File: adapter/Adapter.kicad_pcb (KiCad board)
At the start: 4 copper layers, 33.1 x 18.6 mm, 13 parts, among them J1 USB_B_Micro, J2 2040210-1, J3 USB_C_Receptacle

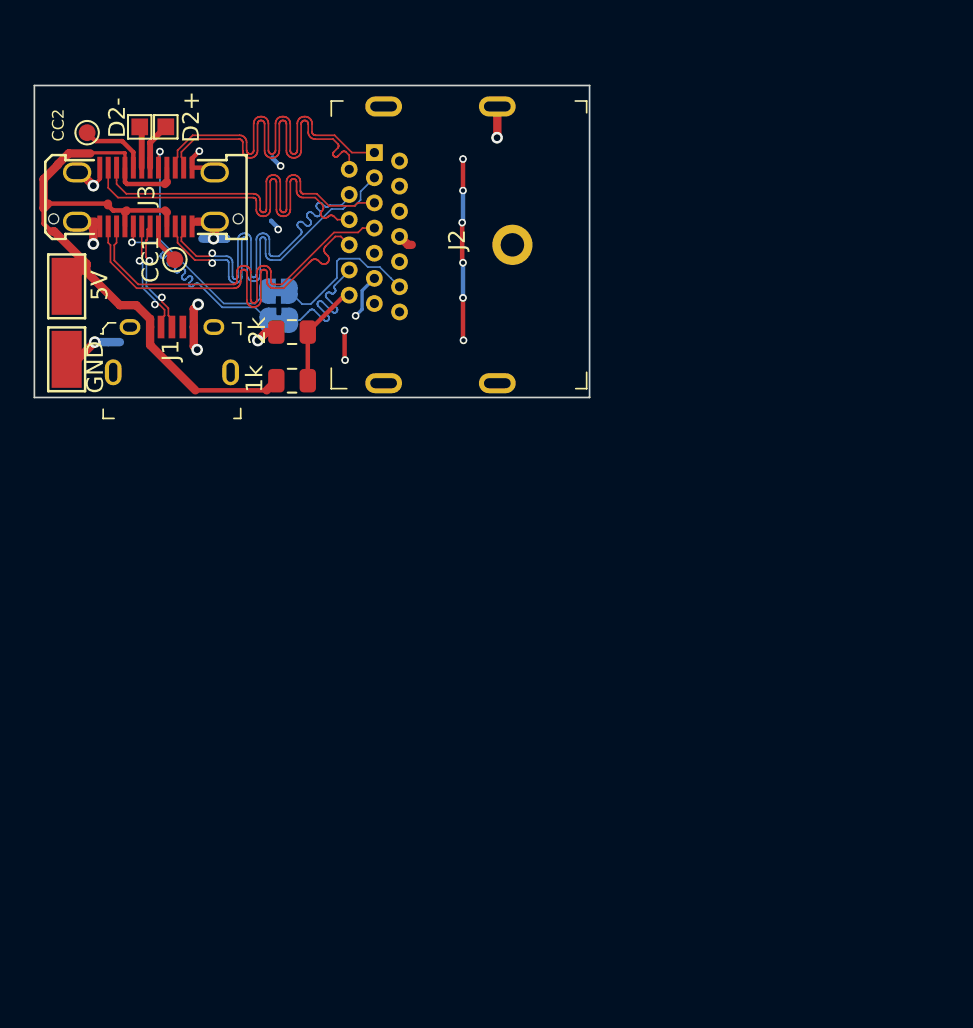
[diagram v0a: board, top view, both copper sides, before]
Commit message: Design considerations and fixed most external circuitry for STM32
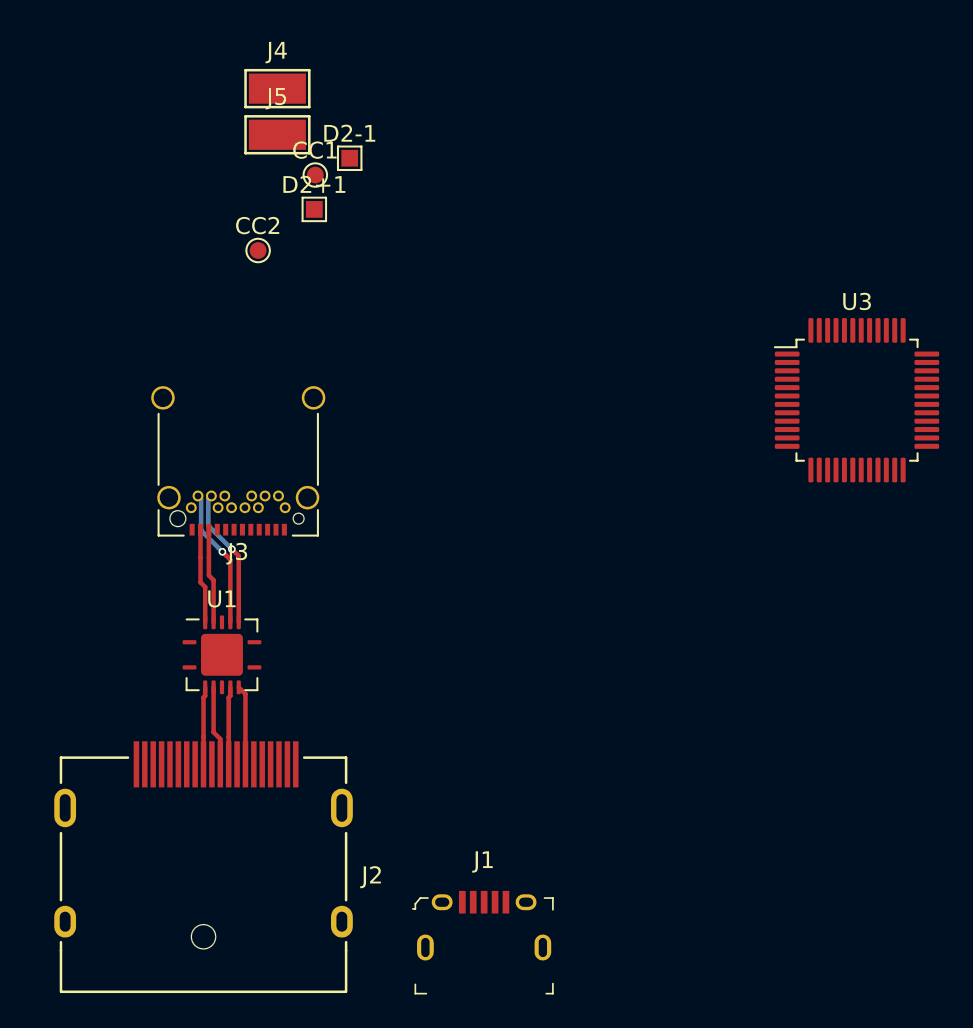
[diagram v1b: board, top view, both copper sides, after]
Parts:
- removed 1k: 1k, Resistor_SMD:R_0805_2012Metric
- removed 2k: 2k, Resistor_SMD:R_0805_2012Metric
- removed 5V, GND: Conn_01x01, TestPoint:TestPoint_Keystone_5015_Micro-Minature
- removed AUX+, AUX-: Jumper, Jumper:SolderJumper-2_P1.3mm_Bridged_RoundedPad1.0x1.5mm
- removed D2+, D2-: Conn_01x01, TestPoint:TestPoint_Pad_1.0x1.0mm
- added D2+1: Conn_01x01, TestPoint:TestPoint_Pad_1.0x1.0mm, F.Cu at (32.5, 21.8)
- added D2-1: Conn_01x01, TestPoint:TestPoint_Pad_1.0x1.0mm, F.Cu at (34.6, 18.8)
- added J4: Conn_01x01, TestPoint:TestPoint_Keystone_5015_Micro-Minature, F.Cu at (30.3, 14.6)
- added J5: Conn_01x01, TestPoint:TestPoint_Keystone_5015_Micro-Minature, F.Cu at (30.3, 17.4)
- added U1: SN75DP119, SN75DP118:QFN-20-1EP_4x4mm_P0.5mm_EP2.5x2.5mm, F.Cu at (27.0, 48.4)
- added U3: STM32F072C8Tx, Package_QFP:LQFP-48_7x7mm_P0.5mm, F.Cu at (64.9, 33.2)
- J2: footprint digikey-footprints:DisplayPort_2040210-1 -> DP1RD20JQ1R400:DP1RD20JQ1R400
- J3: footprint USB_C:DX07S024WJ3R400 -> Connector_USB:USB_C_Receptacle_Amphenol_12401548E4-2A_CircularHoles
- moved J1 39.0 mm to (42.6, 63.1)
- moved J2 38.3 mm to (25.9, 57.5), turned to 0 degrees
- moved J3 14.6 mm to (28.0, 35.9)
- moved CC2 12.4 mm to (29.2, 24.3), turned to 0 degrees
- moved CC1 9.78 mm to (32.6, 19.8), turned to 0 degrees
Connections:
- J2 pad 1: /DP3- -> /DP_IN_3-
- J2 pad 10: /DP0- -> /DP_IN_0-
- J2 pad 12: /DP0+ -> /DP_IN_0+
- J2 pad 3: /DP3+ -> /DP_IN_3+
- J2 pad 4: /DP2- -> /DP_IN_2-
- J2 pad 6: /DP2+ -> /DP_IN_2+
- J2 pad 7: /DP1- -> /DP_IN_1-
- J2 pad 9: /DP1+ -> /DP_IN_1+
- J3 pad A10: /DP0- -> /DP_OUT_0-
- J3 pad A11: /DP0+ -> /DP_OUT_0+
- J3 pad A2: /DP2+ -> Net-(J3-PadA2)
- J3 pad A3: /DP2- -> Net-(J3-PadA3)
- J3 pad A8: /pAUX+ -> /AUX+
- J3 pad B10: /DP3- -> Net-(J3-PadB10)
- J3 pad B11: /DP3+ -> Net-(J3-PadB11)
- J3 pad B2: /DP1+ -> /DP_OUT_1+
- J3 pad B3: /DP1- -> /DP_OUT_1-
- J3 pad B6: /D2+ -> /D+
- J3 pad B7: /D2- -> /D-
- J3 pad B8: /pAUX- -> /AUX-
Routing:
- net VBUS: track 44.2 -> 0.00 mm
- net GND: track 41.0 -> 0.00 mm, vias 20 -> 0
- net /DP0+: track 25.3 -> 0.00 mm
- net /DP0-: track 25.3 -> 0.00 mm
- net /DP2-: track 25.2 -> 0.00 mm, vias 1 -> 0
- net /DP2+: track 25.2 -> 0.00 mm, vias 1 -> 0
- net /DP3+: track 25.1 -> 0.00 mm
- net /DP3-: track 25.1 -> 0.00 mm
- net /DP1+: track 24.8 -> 0.00 mm
- net /DP1-: track 24.6 -> 0.00 mm
- net /pAUX+: track 14.5 -> 0.00 mm, vias 1 -> 0
- net /pAUX-: track 14.5 -> 0.00 mm, vias 1 -> 0
- net /AUX+: track 9.34 -> 0.00 mm
- net /AUX-: track 9.29 -> 0.00 mm
- net /DP_OUT_1-: track 0.00 -> 8.36 mm, vias 0 -> 1
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- removed copper zone on In1.Cu, net GND
- removed copper zone on In2.Cu, net GND
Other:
- board outline removed

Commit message: cleared a bunch of questions
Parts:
- removed J5: Conn_01x01, TestPoint:TestPoint_Keystone_5015_Micro-Minature
- added R8: NF, Resistor_SMD:R_0603_1608Metric_Pad1.05x0.95mm_HandSolder, F.Cu at (44.7, 47.3)
- added R9: NF, Resistor_SMD:R_0603_1608Metric_Pad1.05x0.95mm_HandSolder, F.Cu at (48.1, 45.8)
- J4: value Conn_01x01 -> Conn_01x05_Male
- moved U3 30.6 mm to (37.7, 47.3)
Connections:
- net Net-(U3-Pad21) renamed VBUS_EN
- net Net-(U3-Pad7) renamed /nRESET
- J2 pad 13: /CONFIG1 -> CONFIG1
- J2 pad 14: /CONFIG2 -> CONFIG2
- J3 pad A4: VBUS -> Net-(J3-PadA4)
- J3 pad A9: VBUS -> Net-(J3-PadA4)
- J3 pad B4: VBUS -> Net-(J3-PadA4)
- J3 pad B9: VBUS -> Net-(J3-PadA4)
- J4 pad 1: VBUS -> /EXT_3.3V
- U3 pad 1: Net-(U3-Pad1) -> Net-(C5-Pad2)
- U3 pad 24: Net-(U3-Pad24) -> Net-(C5-Pad2)
- U3 pad 30: Net-(U3-Pad30) -> /HPD
- U3 pad 36: Net-(U3-Pad36) -> Net-(C5-Pad2)
- U3 pad 45: Net-(U3-Pad45) -> CONFIG2
- U3 pad 46: Net-(U3-Pad46) -> CONFIG1
- U3 pad 48: Net-(U3-Pad48) -> Net-(C5-Pad2)
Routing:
- net /D+: track 0.00 -> 45.3 mm
- net /D-: track 0.00 -> 44.7 mm

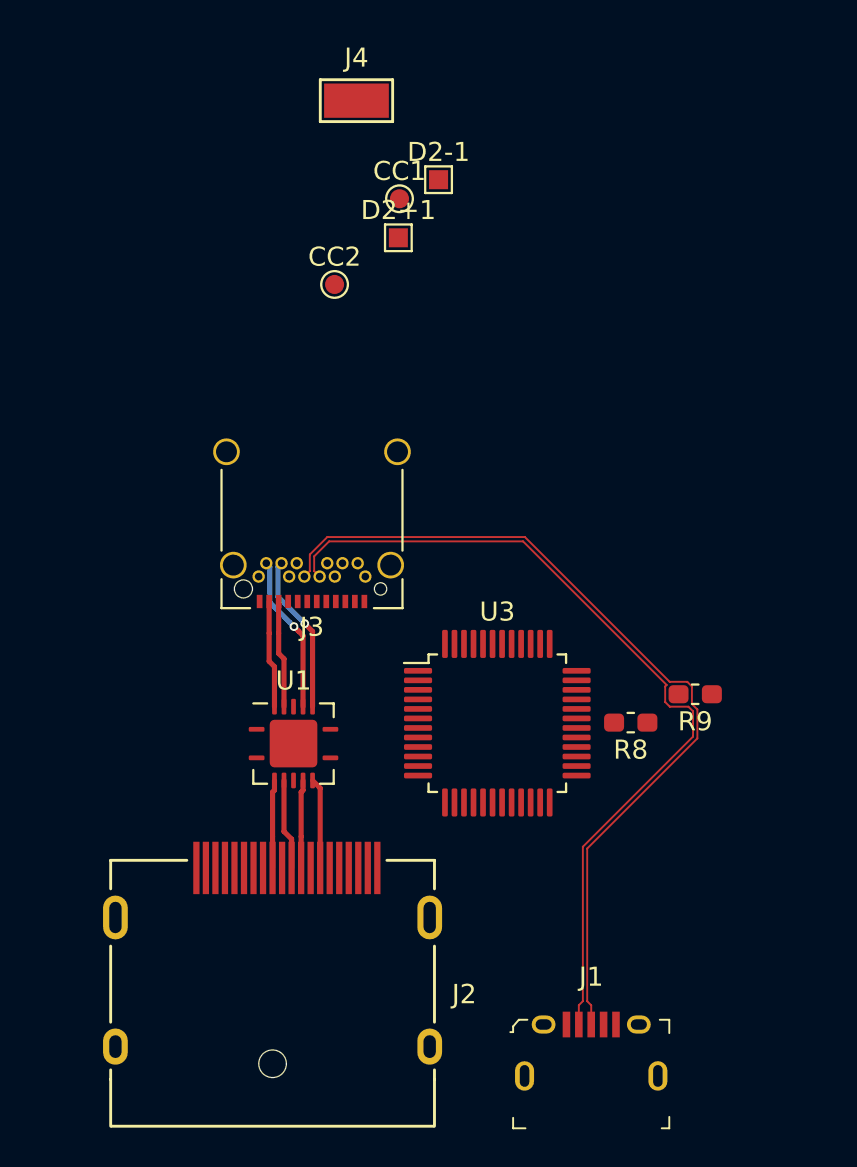
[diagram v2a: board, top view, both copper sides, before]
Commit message: pre-place most of components
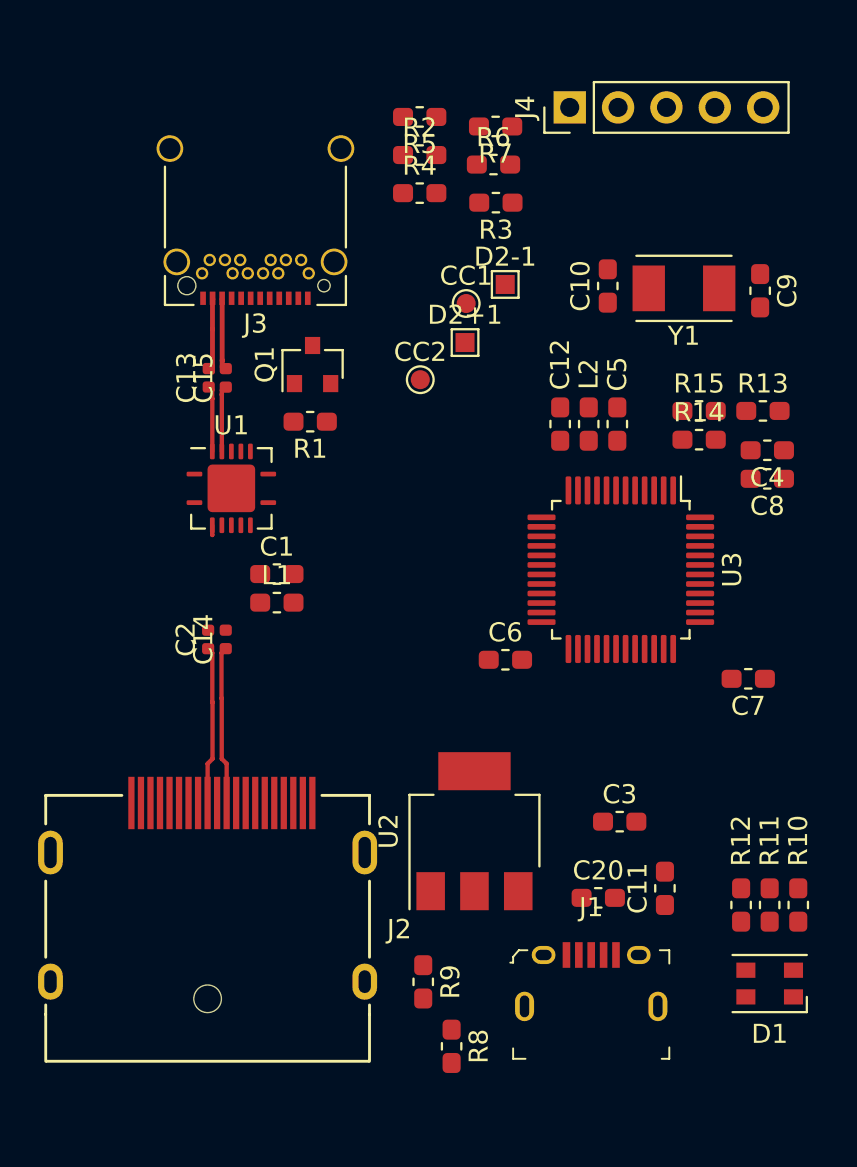
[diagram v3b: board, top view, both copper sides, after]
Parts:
- added C1: 100n, Capacitor_SMD:C_0603_1608Metric_Pad1.05x0.95mm_HandSolder, F.Cu at (26.1, 39.5)
- added C10: 20p, Capacitor_SMD:C_0603_1608Metric_Pad1.05x0.95mm_HandSolder, F.Cu at (43.5, 24.4)
- added C11: 4u7, Capacitor_SMD:C_0603_1608Metric_Pad1.05x0.95mm_HandSolder, F.Cu at (46.5, 56.0)
- added C12: 1u, Capacitor_SMD:C_0603_1608Metric_Pad1.05x0.95mm_HandSolder, F.Cu at (41.0, 31.6)
- added C13: 100n, Capacitor_SMD:C_0402_1005Metric, F.Cu at (22.5, 29.2)
- added C14: 100n, Capacitor_SMD:C_0402_1005Metric, F.Cu at (23.4, 42.9)
- added C15: 100n, Capacitor_SMD:C_0402_1005Metric, F.Cu at (23.4, 29.2)
- added C2: 100n, Capacitor_SMD:C_0402_1005Metric, F.Cu at (22.5, 42.9)
- added C20: 4u7, Capacitor_SMD:C_0603_1608Metric_Pad1.05x0.95mm_HandSolder, F.Cu at (43.0, 56.5)
- added C3: 4u7, Capacitor_SMD:C_0603_1608Metric_Pad1.05x0.95mm_HandSolder, F.Cu at (44.1, 52.5)
- added C4: 100n, Capacitor_SMD:C_0603_1608Metric_Pad1.05x0.95mm_HandSolder, F.Cu at (51.9, 33.0)
- added C5: 100n, Capacitor_SMD:C_0603_1608Metric_Pad1.05x0.95mm_HandSolder, F.Cu at (44.0, 31.6)
- added C6: 100n, Capacitor_SMD:C_0603_1608Metric_Pad1.05x0.95mm_HandSolder, F.Cu at (38.1, 44.0)
- added C7: 100n, Capacitor_SMD:C_0603_1608Metric_Pad1.05x0.95mm_HandSolder, F.Cu at (50.9, 45.0)
- added C8: 100n, Capacitor_SMD:C_0603_1608Metric_Pad1.05x0.95mm_HandSolder, F.Cu at (51.9, 34.5)
- added C9: 20p, Capacitor_SMD:C_0603_1608Metric_Pad1.05x0.95mm_HandSolder, F.Cu at (51.5, 24.6)
- added D1: LED_ARGB, LED_SMD:LED_Cree-PLCC4_3.2x2.8mm_CCW, F.Cu at (52.0, 61.0)
- added L1: CIM05U601NC, Inductor_SMD:L_0603_1608Metric_Pad1.05x0.95mm_HandSolder, F.Cu at (26.1, 41.0)
- added L2: CIM05U601NC, Inductor_SMD:L_0603_1608Metric_Pad1.05x0.95mm_HandSolder, F.Cu at (42.5, 31.6)
- added Q1: IRLML2244TRPBF, Package_TO_SOT_SMD:SOT-23, F.Cu at (28.0, 28.5)
- added R1: 100k, Resistor_SMD:R_0603_1608Metric_Pad1.05x0.95mm_HandSolder, F.Cu at (27.9, 31.5)
- added R10: R, Resistor_SMD:R_0603_1608Metric_Pad1.05x0.95mm_HandSolder, F.Cu at (53.5, 56.9)
- added R11: R, Resistor_SMD:R_0603_1608Metric_Pad1.05x0.95mm_HandSolder, F.Cu at (52.0, 56.9)
- added R12: R, Resistor_SMD:R_0603_1608Metric_Pad1.05x0.95mm_HandSolder, F.Cu at (50.5, 56.9)
- added R13: R, Resistor_SMD:R_0603_1608Metric_Pad1.05x0.95mm_HandSolder, F.Cu at (51.6, 30.9)
- added R14: R, Resistor_SMD:R_0603_1608Metric_Pad1.05x0.95mm_HandSolder, F.Cu at (48.3, 32.4)
- added R15: R, Resistor_SMD:R_0603_1608Metric_Pad1.05x0.95mm_HandSolder, F.Cu at (48.3, 30.9)
- added R2: <5k?, Resistor_SMD:R_0603_1608Metric_Pad1.05x0.95mm_HandSolder, F.Cu at (33.6, 17.5)
- added R3: <5k?, Resistor_SMD:R_0603_1608Metric_Pad1.05x0.95mm_HandSolder, F.Cu at (37.6, 20.0)
- added R4: 200, Resistor_SMD:R_0603_1608Metric_Pad1.05x0.95mm_HandSolder, F.Cu at (33.6, 19.5)
- added R5: 100, Resistor_SMD:R_0603_1608Metric_Pad1.05x0.95mm_HandSolder, F.Cu at (33.6, 15.5)
- added R6: 200, Resistor_SMD:R_0603_1608Metric_Pad1.05x0.95mm_HandSolder, F.Cu at (37.5, 18.0)
- added R7: 100, Resistor_SMD:R_0603_1608Metric_Pad1.05x0.95mm_HandSolder, F.Cu at (37.6, 16.0)
- added U2: AZ1117-3.3, Package_TO_SOT_SMD:SOT-223, F.Cu at (36.5, 53.0)
- added Y1: 8MHZ, Crystal:Crystal_SMD_TXC_7A-2Pin_5x3.2mm, F.Cu at (47.5, 24.5)
- J4: footprint TestPoint:TestPoint_Keystone_5015_Micro-Minature -> Connector_PinHeader_2.54mm:PinHeader_1x05_P2.54mm_Vertical
- moved R9 20.8 mm to (33.8, 60.9), turned to 270 degrees
- moved R8 19.4 mm to (35.3, 64.3), turned to 270 degrees
- moved J3 16.2 mm to (25.0, 20.0)
- moved U1 13.8 mm to (23.7, 35.0)
- moved J4 11.2 mm to (41.5, 15.0), turned to 90 degrees
- moved U3 10.3 mm to (44.2, 39.3), turned to 270 degrees
- moved CC2 6.73 mm to (33.7, 29.3)
- moved CC1 6.52 mm to (36.1, 25.3)
- moved D2+1 6.52 mm to (36.0, 27.3)
- moved D2-1 6.52 mm to (38.1, 24.3)
- moved J2 4.82 mm to (22.5, 54.1)
- moved J1 3.65 mm to (42.6, 59.5)
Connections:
- net Net-(C5-Pad2) renamed +3V3
- net Net-(U3-Pad31) renamed /UART_RX
- U1 pad 10: /DP_OUT_1+ -> Net-(U1-Pad10)
- U1 pad 12: /DP_OUT_0- -> Net-(C15-Pad1)
- U1 pad 13: /DP_OUT_0+ -> Net-(C13-Pad1)
- U1 pad 2: /DP_IN_0+ -> Net-(C2-Pad2)
- U1 pad 3: /DP_IN_0- -> Net-(C14-Pad2)
- U1 pad 5: /DP_IN_1+ -> Net-(U1-Pad5)
- U1 pad 6: /DP_IN_1- -> Net-(U1-Pad6)
- U1 pad 9: /DP_OUT_1- -> Net-(U1-Pad9)
- U3 pad 10: Net-(U3-Pad10) -> /CC1_EN
- U3 pad 11: Net-(U3-Pad11) -> /CC1_RX
- U3 pad 12: Net-(U3-Pad12) -> /CC2_EN
- U3 pad 13: Net-(U3-Pad13) -> /CC2_RX
- U3 pad 14: Net-(U3-Pad14) -> PRE_CTL
- U3 pad 15: Net-(U3-Pad15) -> /TX_CLK
- U3 pad 16: Net-(U3-Pad16) -> /CC2_TX
- U3 pad 17: Net-(U3-Pad17) -> VOD_CTL
- U3 pad 18: Net-(U3-Pad18) -> EQ_CTL
- U3 pad 19: Net-(U3-Pad19) -> EN_CTL
- U3 pad 22: Net-(U3-Pad22) -> /LED_G_L
- U3 pad 23: Net-(U3-Pad23) -> GND
- U3 pad 26: Net-(U3-Pad26) -> /LED_R_L
- U3 pad 27: Net-(U3-Pad27) -> /LED_B_L
- U3 pad 29: Net-(U3-Pad29) -> /HPD
- U3 pad 30: /HPD -> /UART_TX
- U3 pad 35: Net-(U3-Pad35) -> GND
- U3 pad 40: Net-(U3-Pad40) -> /CC1_TX
- U3 pad 43: Net-(U3-Pad43) -> CONFIG1
- U3 pad 44: Net-(U3-Pad44) -> /BOOT
- U3 pad 46: CONFIG1 -> /TX_CLK
- U3 pad 47: Net-(U3-Pad47) -> GND
- U3 pad 8: Net-(U3-Pad8) -> GND
- U3 pad 9: Net-(C6-Pad2) -> VDDA
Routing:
- net /D+: track 45.3 -> 0.00 mm
- net /D-: track 44.7 -> 0.00 mm
- net /DP_OUT_1-: track 8.36 -> 0.00 mm, vias 1 -> 0
- net /DP_OUT_1+: track 8.33 -> 0.00 mm, vias 1 -> 0
- net /DP_IN_1-: track 4.76 -> 0.00 mm
- net /DP_IN_1+: track 4.63 -> 0.00 mm
- net /DP_IN_0+: track 4.63 -> 8.30 mm
- net Net-(C15-Pad1): track 0.00 -> 3.61 mm
- net Net-(C13-Pad1): track 0.00 -> 3.58 mm
- net /DP_IN_0-: track 4.76 -> 8.31 mm
- net /DP_OUT_0-: track 5.64 -> 3.48 mm
- net /DP_OUT_0+: track 5.64 -> 4.06 mm
- net Net-(C2-Pad2): track 0.00 -> 0.51 mm
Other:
- net class DisplayPort added: clearance 0.127, trace_width 0.2286, via_dia 0.46, via_drill 0.26
- net class Power removed

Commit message: Added 3D STEP for micro-USB Jack
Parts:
- removed D2+1, D2-1: Conn_01x01, TestPoint:TestPoint_Pad_1.0x1.0mm
- added C16: 100n, Capacitor_SMD:C_0603_1608Metric_Pad1.05x0.95mm_HandSolder, F.Cu at (41.2, 24.3)
- added R16: 390, Resistor_SMD:R_0603_1608Metric_Pad1.05x0.95mm_HandSolder, F.Cu at (52.1, 32.0)
- added SW1: SW_Push, Button_Switch_SMD:SW_SPST_PTS645, F.Cu at (47.8, 23.0)
- moved J4 37.9 mm to (15.8, 42.8), turned to 180 degrees
- moved R8 30.5 mm to (30.3, 34.2), turned to 0 degrees
- moved R9 25.2 mm to (31.6, 35.8), turned to 0 degrees
- moved C7 17.9 mm to (33.4, 41.3), turned to 90 degrees
- moved C9 17.1 mm to (52.2, 41.7), turned to 180 degrees
- moved C6 15.9 mm to (34.4, 28.5), turned to 270 degrees
- moved Y1 14.0 mm to (52.1, 37.7), turned to 90 degrees
- moved C10 12.8 mm to (52.2, 33.7), turned to 0 degrees
- moved R13 11.9 mm to (47.5, 42.0), turned to 270 degrees
- moved C4 11.3 mm to (45.4, 42.3), turned to 90 degrees
- moved C8 11.1 mm to (43.9, 42.3), turned to 90 degrees
- moved R15 7.80 mm to (47.5, 38.7), turned to 270 degrees
- moved CC2 7.77 mm to (37.6, 22.6)
- moved U3 6.89 mm to (39.1, 34.6), turned to 180 degrees
- moved C20 6.77 mm to (46.1, 50.5)
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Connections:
- U3 pad 6: Net-(C10-Pad1) -> Net-(R16-Pad1)
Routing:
- net /D-: track 0.00 -> 28.7 mm, vias 0 -> 1
- net /D+: track 0.00 -> 28.6 mm
- net Net-(C2-Pad2): track 0.51 -> 6.12 mm
- net Net-(C14-Pad2): track 0.00 -> 5.59 mm
- net Net-(C1-Pad1): track 0.00 -> 4.69 mm

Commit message: Step file for MicroUSB
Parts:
- added R17: 0, Resistor_SMD:R_0603_1608Metric_Pad1.05x0.95mm_HandSolder, F.Cu at (43.8, 47.7)
- added SW2: SW_Push, Button_Switch_SMD:SW_SPST_PTS645, F.Cu at (-47.1, -2.67)
- J1: footprint digikey-footprints:USB_Micro_B_Female_10118194-0001LF -> USB_MicroB:CONN-10118194-0001LF-FCI
- J3: footprint Connector_USB:USB_C_Receptacle_Amphenol_12401548E4-2A_CircularHoles -> Connector_USB:USB_C_Receptacle_Amphenol_12401610E4-2A
- R13, R15: value R -> 100k
- R14: value R -> 0
- R8, R9: value NF -> 0
- moved D1 100.5 mm to (-31.1, 4.50)
- moved R10 100.5 mm to (-29.6, 0.38)
- moved R11 100.5 mm to (-31.1, 0.38)
- moved R12 100.5 mm to (-32.6, 0.38)
- moved SW1 96.6 mm to (-47.2, 5.30)
- moved C1 36.4 mm to (57.3, 58.3)
- moved C14 36.4 mm to (54.6, 61.7)
- moved C2 36.4 mm to (53.7, 61.7)
- moved J2 36.4 mm to (53.7, 72.9)
- moved J3 36.4 mm to (56.2, 38.8)
- moved L1 36.4 mm to (57.3, 59.8)
- moved Q1 36.4 mm to (59.2, 47.3)
- moved R1 36.4 mm to (59.1, 50.3)
- moved U1 36.4 mm to (54.9, 53.8)
- moved C13 36.4 mm to (53.7, 48.0)
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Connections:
- R14 pad 1: +3V3 -> /AUX-
- R14 pad 2: /BOOT -> Net-(R14-Pad2)
- U3 pad 10: /CC1_EN -> EN_CTL
- U3 pad 12: /CC2_EN -> PRE_CTL
- U3 pad 14: PRE_CTL -> Net-(R14-Pad2)
- U3 pad 15: /TX_CLK -> Net-(R17-Pad2)
- U3 pad 19: EN_CTL -> /TX_CLK
- U3 pad 34: Net-(U3-Pad34) -> /SWDIO
- U3 pad 37: Net-(U3-Pad37) -> /SWCLK
- U3 pad 39: Net-(U3-Pad39) -> /TX_CLK
- U3 pad 41: Net-(U3-Pad41) -> /CC1_EN
- U3 pad 42: Net-(U3-Pad42) -> /CC2_EN
- U3 pad 46: /TX_CLK -> Net-(U3-Pad46)
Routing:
- net GND: track 0.00 -> 5.65 mm
- net /D+: track 28.6 -> 27.0 mm
- net /D-: track 28.7 -> 27.1 mm, vias 1 -> 0
- net Net-(J3-PadA4): track 0.00 -> 0.96 mm, vias 0 -> 1

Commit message: sync changs from tmp checkout
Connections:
- net /DP_OUT_1+ renamed Net-(J3-PadB2)
- net /DP_OUT_1- renamed Net-(J3-PadB3)
- J1 pad SH: (no net) -> GND
- J2 pad 13: CONFIG1 -> /CONFIG1
- J2 pad 14: CONFIG2 -> /CONFIG2
- U3 pad 43: CONFIG1 -> Net-(U3-Pad43)
- U3 pad 45: CONFIG2 -> Net-(U3-Pad45)
